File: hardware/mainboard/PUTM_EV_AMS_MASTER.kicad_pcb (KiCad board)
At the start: 4 copper layers, 60 x 100 mm, 126 parts, among them IC3 BQ79600PWRQ1, IC6 AMC3330DWER, IC7 AMC3330DWER, IC8 ADC 24bit, IC9 LTC1799, J1 Conn_02x10_Odd_Even, J10 M300-MV10345M1, J3 Conn_02x04_Odd_Even, J4 FTSH-107-01-L-D-K, J5 M80-51004XX, J7 M300-MV10345M1, J8 M80-51004XX, Q6 2N7002, Q8 2N7002, Q9 2N7002, T1 SM91502ALE, U10 STM32H573RITx, U3 74AUP1G32

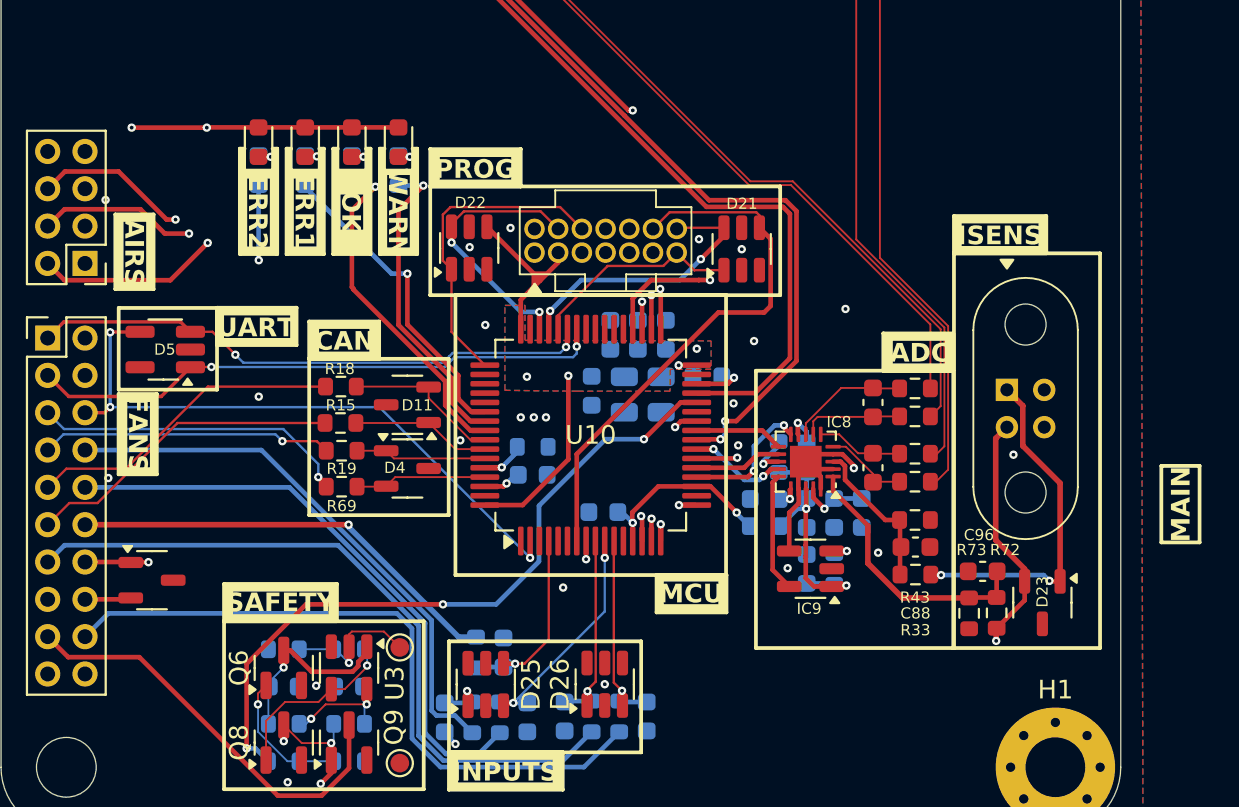
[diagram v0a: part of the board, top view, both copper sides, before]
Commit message: Fixed silkscreen oopsie
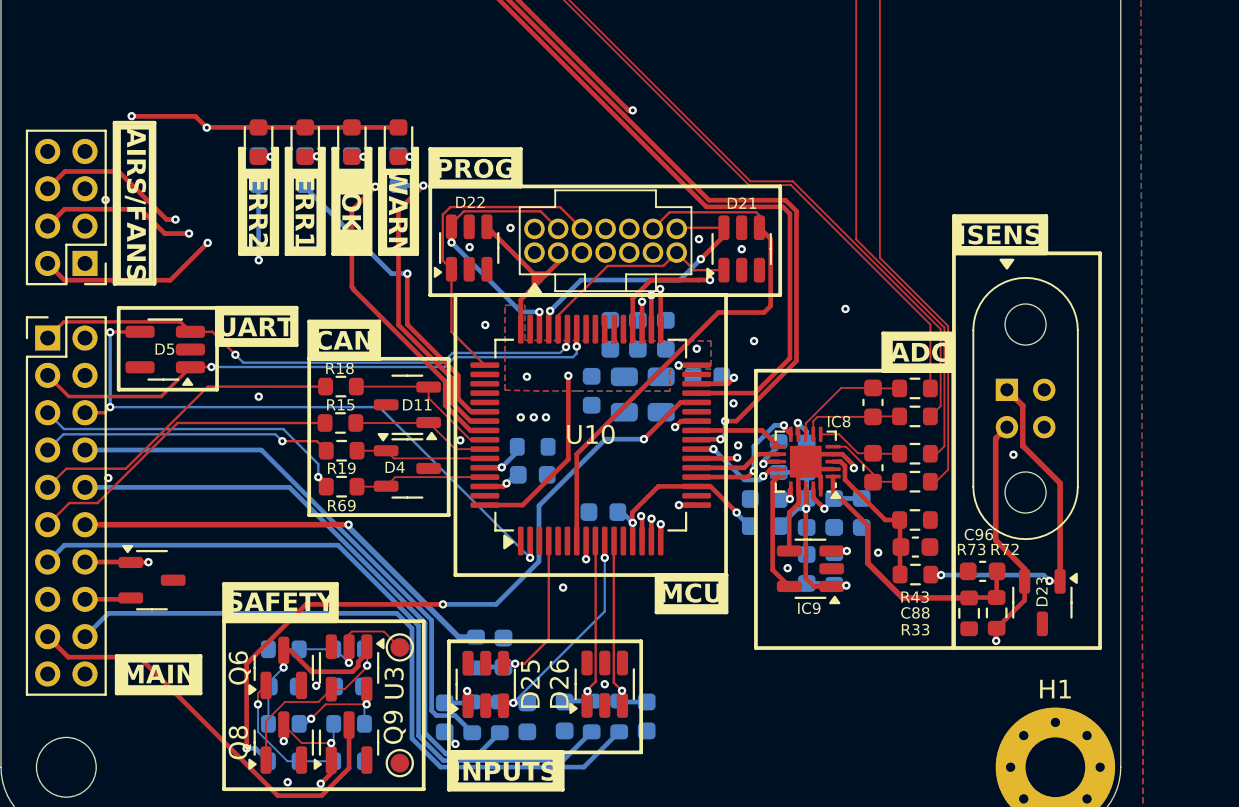
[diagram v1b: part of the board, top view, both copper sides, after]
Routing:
- net +3.3VIO: track 126.7 -> 127.6 mm
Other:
- board text added: "AIRS/FANS"
- board text removed: "AIRS"
- board text removed: "FANS"
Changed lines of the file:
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@@
 			(at 1 8.11 0)
 			(layer "F.Fab")
+			(hide yes)
 			(effects
 				(font
@@
 			(at 1 20.11 0)
 			(layer "F.Fab")
+			(hide yes)
 			(effects
 				(font
@@
 	)
 	(gr_rect
-		(start 164.175 128.35)
-		(end 166.225 132.45)
+		(start 108.2 138.54)
+		(end 112.69 140.54)
 		(stroke
 			(width 0.2)
@@
 		(layer "F.SilkS")
 	)
-	(gr_rect
-		(start 108.3 124.5)
-		(end 110.35 128.8)
-		(stroke
-			(width 0.2)
-			(type default)
-		)
-		(fill no)
-		(layer "F.SilkS")
-	)
 	(gr_line
 		(start 117.3 117)
@@
 	)
 	(gr_rect
-		(start 108.125 114.875)
-		(end 110.175 118.875)
+		(start 108.085 109.96)
+		(end 110.225 118.59)
 		(stroke
 			(width 0.2)
@@
 	)
 	(gr_text "MAIN"
-		(at 165.225 130.4 90)
+		(at 110.445 139.54 0)
 		(layer "F.SilkS" knockout)
 		(effects
@@
 		)
 	)
-	(gr_text "FANS"
-		(at 109.325 126.65 270)
-		(layer "F.SilkS" knockout)
-		(effects
-			(font
-				(size 1 1)
-				(thickness 0.2)
-				(bold yes)
-			)
-		)
-	)
 	(gr_text "PROG"
 		(at 127.4 112.45 0)
@@
 		)
 	)
-	(gr_text "AIRS"
-		(at 109.125 116.925 270)
+	(gr_text "AIRS/FANS"
+		(at 109.22 114.36 270)
 		(layer "F.SilkS" knockout)
 		(effects
@@
 	)
 	(segment
+		(start 113.025 110.225)
+		(end 112.42 109.62)
+		(width 0.25)
+		(layer "F.Cu")
+		(net 74)
+	)
+	(segment
 		(start 145.12 134.37)
 		(end 145.12 133.224402)
@@
 	)
 	(segment
-		(start 145.12 132.596598)
-		(end 145.12 130.672)
+		(start 112.42 109.62)
+		(end 109.01 109.62)
 		(width 0.25)
 		(layer "F.Cu")
@@
 	)
 	(segment
-		(start 147.298 134.7605)
-		(end 146.5605 134.7605)
+		(start 145.12 132.596598)
+		(end 145.12 130.672)
 		(width 0.25)
 		(layer "F.Cu")
@@
 	)
 	(segment
-		(start 113.025 110.225)
-		(end 109 110.225)
+		(start 147.298 134.7605)
+		(end 146.5605 134.7605)
 		(width 0.25)
 		(layer "F.Cu")
@@
 	)
 	(segment
+		(start 109.01 109.62)
+		(end 109 109.61)
+		(width 0.25)
+		(layer "F.Cu")
+		(net 74)
+	)
+	(segment
 		(start 146.5605 134.7605)
 		(end 146.5105 134.8105)
@@
 	)
 	(via
-		(at 109 110.225)
+		(at 109 109.61)
 		(size 0.45)
 		(drill 0.2)
@@
 	)
 	(segment
-		(start 106.5 133.5)
-		(end 109 131)
-		(width 0.25)
-		(layer "In1.Cu")
-		(net 74)
-	)
-	(segment
 		(start 145.146 130.646)
 		(end 145.146 131.124612)
@@
 	)
 	(segment
-		(start 109 131)
-		(end 109 110.225)
+		(start 145.146 131.124612)
+		(end 138.220612 138.05)
 		(width 0.25)
 		(layer "In1.Cu")
@@
 	)
 	(segment
-		(start 145.146 131.124612)
-		(end 138.220612 138.05)
+		(start 135.58 138.05)
+		(end 114.44 138.05)
 		(width 0.25)
 		(layer "In1.Cu")
@@
 	)
 	(segment
-		(start 135.58 138.05)
-		(end 114.44 138.05)
+		(start 109 131)
+		(end 106.5 133.5)
 		(width 0.25)
 		(layer "In1.Cu")
@@
 	)
 	(segment
+		(start 109 109.61)
+		(end 109 131)
+		(width 0.25)
+		(layer "In1.Cu")
+		(net 74)
+	)
+	(segment
 		(start 114.44 138.05)
 		(end 109.9 133.51)
@@
 		(polygon
 			(pts
-				(xy 108 54.35) (xy 108 56.35) (xy 112.05 56.35) (xy 112.05 54.35)
+				(xy 112.69 140.5625) (xy 112.69 138.5625) (xy 108.24 138.5725) (xy 108.24 140.5725)
 			)
 		)
@@
 		(polygon
 			(pts
-				(xy 166.175 128.35) (xy 164.175 128.35) (xy 164.175 132.45) (xy 166.175 132.45)
+				(xy 108 54.35) (xy 108 56.35) (xy 112.05 56.35) (xy 112.05 54.35)
 			)
 		)
@@
 		(polygon
 			(pts
-				(xy 108.3 128.8) (xy 110.35 128.8) (xy 110.35 124.5) (xy 108.3 124.5)
-			)
-		)
-	)
-	(zone
-		(net 0)
-		(net_name "")
-		(layer "F.SilkS")
-		(hatch edge 0.5)
-		(connect_pads
-			(clearance 0)
-		)
-		(min_thickness 0)
-		(filled_areas_thickness no)
-		(fill yes
-			(thermal_gap 0.5)
-			(thermal_bridge_width 0.5)
-		)
-		(polygon
-			(pts
 				(xy 129.75 54.55) (xy 129.75 56.55) (xy 133.25 56.55) (xy 133.25 54.55)
 			)
@@
 		(polygon
 			(pts
-				(xy 108.175 118.875) (xy 110.175 118.875) (xy 110.175 114.875) (xy 108.175 114.875)
+				(xy 108.134906 118.49) (xy 110.134906 118.49) (xy 110.154906 110.04) (xy 108.154906 110.04)
 			)
 		)

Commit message: Layout ver.2
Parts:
- added J2: XIAO ESP32S3 Sense, xiao:XIAO-ESP32-S3-DIP, F.Cu at (145.0, 135.8)
- added U1: MAX40200AUK, Package_TO_SOT_SMD:SOT-23-5_HandSoldering, F.Cu at (138.5, 123.6)
- C10, C101, C102, C103, C104, C105, C23, C24, C25, C28, C29, C36, C43, C45, C46, C47, C48, C52, C53, C55, C7, C70, C78, C8, C81, C86, C87, C9, C93, C98, C99, R100, R11, R12, R13, R14, R17, R20, R21, R22, R24, R25, R26, R27, R3, R31, R34, R36, R38, R9, R93, R99: moved to F.Cu
- D1, D6: value LED -> LED_R
- D3: value LED -> LED_G
- moved R33 55.5 mm to (151.0, 78.7)
- moved C88 54.8 mm to (148.8, 77.9), turned to -90 degrees
- moved R43 53.5 mm to (147.3, 77.9), turned to -90 degrees
- moved R50 52.2 mm to (141.5, 77.9), turned to 90 degrees
- moved R51 51.0 mm to (140.0, 77.9), turned to -90 degrees
- moved C52 50.1 mm to (151.8, 84.3)
- moved R24 49.7 mm to (150.3, 84.3)
- moved IC9 49.7 mm to (147.5, 84.2)
- moved R52 49.5 mm to (138.0, 77.9), turned to 90 degrees
- moved C89 49.0 mm to (140.7, 80.1), turned to 0 degrees
- moved C45 48.8 mm to (143.3, 82.2), turned to 90 degrees
- moved C46 48.8 mm to (144.7, 82.2), turned to 90 degrees
- moved R54 48.5 mm to (136.5, 77.9), turned to -90 degrees
- moved C90 46.3 mm to (137.2, 80.1), turned to 0 degrees
- moved TP4 45.2 mm to (115.0, 99.8)
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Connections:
- U10 pad 37: unconnected-(U10-PC6-Pad37) -> /MCU/LOG_UART_TX
- U10 pad 38: unconnected-(U10-PC7-Pad38) -> /MCU/LOG_UART_RX
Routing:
- net +5VIO: track 145.9 -> 11.6 mm, vias 6 -> 0
- net +3.3VIO: track 127.6 -> 27.7 mm, vias 6 -> 0
- net +5VA: track 74.9 -> 12.3 mm, vias 1 -> 0
- net /UCRX: track 57.6 -> 0.00 mm, vias 2 -> 0
- net /UCTX: track 55.8 -> 0.00 mm
- net /ADC/CAR_V+: track 66.3 -> 16.4 mm
- net /ADC/CAR_V-: track 64.8 -> 15.3 mm
- net /ADC/ACU_V+: track 59.6 -> 10.5 mm
- net /ADC/ACU_V-: track 58.5 -> 11.3 mm
- net +3.3VA: track 48.8 -> 3.03 mm, vias 1 -> 0
- net /DETVUSB: track 42.3 -> 0.00 mm, vias 1 -> 0
- net /~{FLT}: track 54.6 -> 13.5 mm, vias 3 -> 1
- net /FAN4-: track 40.6 -> 0.00 mm, vias 1 -> 0
- net /FAN3-: track 39.6 -> 0.00 mm, vias 1 -> 0
- net /TSMS_DETECTION: track 38.5 -> 0.07 mm
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- added copper zone on F.Cu, net +3.3VIO
- added copper zone on F.Cu, net +5VIO
- added copper zone on F.Cu, net /Safety/CAP_VOLT
- added copper zone on F.Cu, net /Safety/CT_G
- added copper zone on F.Cu, net Net-(R14-Pad2)
- removed copper zone on B.Cu, net +3.3VMCU
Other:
- board text added: "LOGGING"

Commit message: New HV layout and also a lazy prolly bad main layout that i didnt think much about yet tbh
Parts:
- removed the H1 at (158.5, 86.5)
- removed the H1 at (158.5, 144.5)
- added H3: M3, MountingHole:MountingHole_3.2mm_M3, F.Cu at (158.5, 144.5)
- C16, C18, C54, C59, C67, C77, C91, C92, C94, C95, R64, R65, R66, R67: moved to F.Cu
- D1, D6: value LED_R -> LED
- D3: value LED_G -> LED
- moved G*** 86.5 mm to (47.0, 95.8)
- moved R38 52.8 mm to (160.2, 98.0), turned to 180 degrees
- moved R14 51.3 mm to (160.2, 99.5), turned to 180 degrees
- moved C86 49.2 mm to (139.8, 96.2), turned to 90 degrees
- moved Q9 49.1 mm to (152.7, 95.5), turned to 180 degrees
- moved U3 48.4 mm to (156.6, 99.0), turned to 180 degrees
- moved C7 48.2 mm to (159.1, 101.4), turned to 180 degrees
- moved TP1 47.7 mm to (160.3, 103.3), turned to -90 degrees
- moved TP4 45.7 mm to (160.3, 105.5), turned to -90 degrees
- moved R12 45.3 mm to (156.1, 101.4), turned to 0 degrees
- moved Q8 45.1 mm to (152.7, 99.0), turned to 180 degrees
- moved Q6 42.8 mm to (156.3, 104.1), turned to 90 degrees
- moved R13 42.6 mm to (153.1, 101.4), turned to 0 degrees
- moved C8 41.0 mm to (153.1, 102.9), turned to 0 degrees
- moved R11 39.4 mm to (153.2, 104.3), turned to 180 degrees
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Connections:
- U1 pad 1: +3.3VMCU -> +3.3VIO
- U1 pad 3: +3.3VMCU -> +3.3VIO
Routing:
- net +3.3VMCU: track 55.4 -> 2.80 mm, vias 2 -> 0
- net /ERROR_RELAY-: track 30.3 -> 0.00 mm
- net /NRST: track 29.6 -> 6.80 mm
- net +3.3VIO: track 27.7 -> 50.2 mm
- net /CAR_I: track 20.9 -> 0.00 mm
- net /CRX1: track 3.87 -> 23.3 mm, vias 0 -> 2
- net /CTX1: track 3.87 -> 22.4 mm
- net /CTX2: track 3.91 -> 21.8 mm
- net /CRX2: track 3.89 -> 21.2 mm
- net /ADC/CAR_V+: track 16.4 -> 0.00 mm
- net /ADC/CAR_V-: track 15.3 -> 0.00 mm
- net /MCU/3.3V_PROT: track 17.8 -> 2.77 mm
- net /UART_DBG_TX: track 15.0 -> 2.59 mm, vias 2 -> 0
- net /AED: track 15.6 -> 3.15 mm
- net /ADC/ACU_V-: track 11.3 -> 0.00 mm
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
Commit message: Layout again
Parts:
- added D24: 3.6V/400W, Package_TO_SOT_SMD:SOT-23-6, F.Cu at (109.7, 114.6)
- added D28: 3.6V/400W, Package_TO_SOT_SMD:SOT-23-6, F.Cu at (104.8, 108.2)
- added TP10: TestPoint_Small, TestPoint:TestPoint_Pad_D1.0mm, F.Cu at (189.7, 52.8)
- added TP11: TestPoint_Small, TestPoint:TestPoint_Pad_D1.0mm, F.Cu at (192.7, 46.6)
- added TP12: TestPoint_Small, TestPoint:TestPoint_Pad_D1.0mm, F.Cu at (192.7, 49.7)
- added TP13: TestPoint_Small, TestPoint:TestPoint_Pad_D1.0mm, F.Cu at (192.7, 52.8)
- added TP14: TestPoint_Small, TestPoint:TestPoint_Pad_D1.0mm, F.Cu at (195.8, 46.6)
- added TP15: TestPoint_Small, TestPoint:TestPoint_Pad_D1.0mm, F.Cu at (195.8, 49.7)
- added TP16: TestPoint_Small, TestPoint:TestPoint_Pad_D1.0mm, F.Cu at (195.8, 52.8)
- added TP17: TestPoint_Small, TestPoint:TestPoint_Pad_D1.0mm, F.Cu at (194.7, 57.8)
- added TP18: TestPoint_Small, TestPoint:TestPoint_Pad_D1.0mm, F.Cu at (194.7, 60.9)
- added TP19: TestPoint_Small, TestPoint:TestPoint_Pad_D1.0mm, F.Cu at (175.4, 46.6)
- added TP2: TestPoint_Small, TestPoint:TestPoint_Pad_D1.0mm, F.Cu at (194.7, 65.9)
- added TP20: TestPoint_Small, TestPoint:TestPoint_Pad_D1.0mm, F.Cu at (175.4, 49.7)
- added TP21: TestPoint_Small, TestPoint:TestPoint_Pad_D1.0mm, F.Cu at (175.4, 52.8)
- added TP22: TestPoint_Small, TestPoint:TestPoint_Pad_D1.0mm, F.Cu at (175.4, 55.8)
- added TP23: TestPoint_Small, TestPoint:TestPoint_Pad_D1.0mm, F.Cu at (175.4, 58.9)
- added TP24: TestPoint_Small, TestPoint:TestPoint_Pad_D1.0mm, F.Cu at (175.4, 61.9)
- added TP25: TestPoint_Small, TestPoint:TestPoint_Pad_D1.0mm, F.Cu at (175.4, 65.0)
- added TP26: TestPoint_Small, TestPoint:TestPoint_Pad_D1.0mm, F.Cu at (178.5, 46.6)
- added TP27: TestPoint_Small, TestPoint:TestPoint_Pad_D1.0mm, F.Cu at (178.5, 49.7)
- added TP28: TestPoint_Small, TestPoint:TestPoint_Pad_D1.0mm, F.Cu at (178.5, 52.8)
- added TP29: TestPoint_Small, TestPoint:TestPoint_Pad_D1.0mm, F.Cu at (178.5, 55.8)
- added TP3: TestPoint_Small, TestPoint:TestPoint_Pad_D1.0mm, F.Cu at (194.7, 69.0)
- added TP30: TestPoint_Small, TestPoint:TestPoint_Pad_D1.0mm, F.Cu at (178.5, 58.9)
- added TP31: TestPoint_Small, TestPoint:TestPoint_Pad_D1.0mm, F.Cu at (178.5, 61.9)
- added TP32: TestPoint_Small, TestPoint:TestPoint_Pad_D1.0mm, F.Cu at (178.5, 65.0)
- added TP33: TestPoint_Small, TestPoint:TestPoint_Pad_D1.0mm, F.Cu at (181.6, 46.6)
- added TP34: TestPoint_Small, TestPoint:TestPoint_Pad_D1.0mm, F.Cu at (181.6, 49.7)
- added TP35: TestPoint_Small, TestPoint:TestPoint_Pad_D1.0mm, F.Cu at (181.6, 52.8)
- added TP36: TestPoint_Small, TestPoint:TestPoint_Pad_D1.0mm, F.Cu at (181.6, 55.8)
- added TP37: TestPoint_Small, TestPoint:TestPoint_Pad_D1.0mm, F.Cu at (181.6, 58.9)
- added TP38: TestPoint_Small, TestPoint:TestPoint_Pad_D1.0mm, F.Cu at (181.6, 61.9)
- added TP39: TestPoint_Small, TestPoint:TestPoint_Pad_D1.0mm, F.Cu at (181.6, 65.0)
- added TP40: TestPoint_Small, TestPoint:TestPoint_Pad_D1.0mm, F.Cu at (184.6, 46.6)
- added TP41: TestPoint_Small, TestPoint:TestPoint_Pad_D1.0mm, F.Cu at (184.6, 49.7)
- added TP42: TestPoint_Small, TestPoint:TestPoint_Pad_D1.0mm, F.Cu at (184.6, 52.8)
- added TP43: TestPoint_Small, TestPoint:TestPoint_Pad_D1.0mm, F.Cu at (184.6, 55.8)
- added TP44: TestPoint_Small, TestPoint:TestPoint_Pad_D1.0mm, F.Cu at (184.6, 58.9)
- added TP45: TestPoint_Small, TestPoint:TestPoint_Pad_D1.0mm, F.Cu at (184.6, 61.9)
- added TP5: TestPoint_Small, TestPoint:TestPoint_Pad_D1.0mm, F.Cu at (189.7, 57.8)
- added TP6: TestPoint_Small, TestPoint:TestPoint_Pad_D1.0mm, F.Cu at (189.7, 60.9)
- added TP7: TestPoint_Small, TestPoint:TestPoint_Pad_D1.0mm, F.Cu at (189.7, 63.9)
- added TP8: TestPoint_Small, TestPoint:TestPoint_Pad_D1.0mm, F.Cu at (189.7, 46.6)
- added TP9: TestPoint_Small, TestPoint:TestPoint_Pad_D1.0mm, F.Cu at (189.7, 49.7)
- moved D6 61.7 mm to (103.6, 91.2), turned to 180 degrees
- moved D1 59.9 mm to (103.6, 93.6), turned to 180 degrees
- moved D2 58.6 mm to (103.6, 96.0), turned to 180 degrees
- moved D3 57.6 mm to (103.6, 98.4), turned to 180 degrees
- moved R36 47.9 mm to (111.2, 91.2), turned to 180 degrees
- moved R34 45.8 mm to (111.2, 93.5), turned to 180 degrees
- moved R31 44.0 mm to (111.2, 96.0), turned to 180 degrees
- moved R27 42.6 mm to (111.2, 98.3), turned to 180 degrees
- moved R69 14.7 mm to (119.5, 104.0), turned to 90 degrees
- moved TP4 13.0 mm to (147.3, 106.3), turned to 180 degrees
- moved R19 12.5 mm to (117.6, 104.0), turned to -90 degrees
- moved D4 11.3 mm to (118.6, 100.4), turned to 90 degrees
- moved TP1 11.2 mm to (149.6, 106.3), turned to 180 degrees
- moved R15 10.9 mm to (115.9, 104.0), turned to -90 degrees
- moved R38 9.74 mm to (154.9, 106.2), turned to 90 degrees
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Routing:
- net +3.3VIO: track 50.2 -> 27.2 mm
- net /CRX1: track 23.3 -> 1.58 mm, vias 2 -> 0
- net /CTX1: track 22.4 -> 1.58 mm
- net /CTX2: track 21.8 -> 3.91 mm
- net /CRX2: track 21.2 -> 3.89 mm
- net /AIR_PRE-: track 0.00 -> 11.8 mm
- net /AIR_P-: track 0.00 -> 6.90 mm
- net /IsolationBarrier/ACU_GND: track 3.55 -> 9.82 mm, vias 0 -> 4
- net /IsolationBarrier/ACU_IN+: track 0.00 -> 5.68 mm
- net /FAN4-: track 0.00 -> 5.38 mm
- net /FAN1-: track 0.00 -> 5.29 mm
- net /AIR_M-: track 0.00 -> 4.89 mm
- net +5VIO: track 5.17 -> 8.66 mm
- net /IsolationBarrier/CAR_IN+: track 2.45 -> 5.52 mm
- net /IsolationBarrier/ACU+: track 11.6 -> 8.58 mm
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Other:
- outline, holes or cut-outs redrawn
